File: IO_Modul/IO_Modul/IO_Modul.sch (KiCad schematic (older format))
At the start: 76 parts, among them J101 Conn_02x20_Odd_Even, J102 Screw_Terminal_01x02, J103 Screw_Terminal_01x02, J104 Screw_Terminal_01x02, J105 Screw_Terminal_01x02, J106 Screw_Terminal_01x02, J107 Screw_Terminal_01x02, J108 Screw_Terminal_01x02, J109 Screw_Terminal_01x02, J110 Screw_Terminal_01x02, J111 Screw_Terminal_01x02, J112 Screw_Terminal_01x02, J113 Screw_Terminal_01x02, J114 Screw_Terminal_01x02, J115 Screw_Terminal_01x02, J116 Screw_Terminal_01x02, J117 Screw_Terminal_01x02, J118 Screw_Terminal_01x02, J119 Screw_Terminal_01x02, J120 Screw_Terminal_01x02, J121 Screw_Terminal_01x02, J122 Screw_Terminal_01x02, Q101 Si4431CDY, Q102 Si4431CDY, Q103 Si4431CDY, Q104 Si4431CDY, Q105 Si4431CDY, Q106 2N7002, Q107 2N7002, Q108 2N7002, Q109 2N7002, Q110 2N7002, Q111 Si4431CDY, Q112 Si4431CDY, Q113 Si4431CDY, Q114 Si4431CDY, Q115 Si4431CDY, Q116 2N7002, Q117 2N7002, Q118 2N7002, Q119 2N7002, Q120 2N7002

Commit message: Feeder Microswitch für Tape Motor hinzugefügt. Einige 3D Step Modelle hinzugefügt. Stepper Board die Ecken abgerundet.
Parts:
- J102, J103, J104, J105, J106, J107, J108, J109, J110, J111, J112, J113, J114, J115, J116, J117, J118, J119, J120, J121, J122: footprint TerminalBlock_RND:TerminalBlock_RND_205-00045_1x02_P5.00mm_Horizontal -> ProjectFootprints:TerminalBlock_RND_205-00045_1x02_P5.00mm_Horizontal
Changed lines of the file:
@@
 F 0 "J102" H 1320 785 50  0000 C CNN
 F 1 "Screw_Terminal_01x02" H 1320 876 50  0000 C CNN
-F 2 "TerminalBlock_RND:TerminalBlock_RND_205-00045_1x02_P5.00mm_Horizontal" H 1400 1200 50  0001 C CNN
+F 2 "ProjectFootprints:TerminalBlock_RND_205-00045_1x02_P5.00mm_Horizontal" H 1400 1200 50  0001 C CNN
 F 3 "https://datasheet.lcsc.com/szlcsc/1912251636_Ningbo-Kangnex-Elec-WJ301V-5-0-2P_C8475.pdf" H 1400 1200 50  0001 C CNN
 F 4 "C8475" H 1320 967 50  0000 C CNN "LCSC"
@@
 F 0 "J103" H 1320 1635 50  0000 C CNN
 F 1 "Screw_Terminal_01x02" H 1320 1726 50  0000 C CNN
-F 2 "TerminalBlock_RND:TerminalBlock_RND_205-00045_1x02_P5.00mm_Horizontal" H 1400 2050 50  0001 C CNN
+F 2 "ProjectFootprints:TerminalBlock_RND_205-00045_1x02_P5.00mm_Horizontal" H 1400 2050 50  0001 C CNN
 F 3 "https://datasheet.lcsc.com/szlcsc/1912251636_Ningbo-Kangnex-Elec-WJ301V-5-0-2P_C8475.pdf" H 1400 2050 50  0001 C CNN
 F 4 "C8475" H 1320 1817 50  0000 C CNN "LCSC"
@@
 F 0 "J104" H 1320 2535 50  0000 C CNN
 F 1 "Screw_Terminal_01x02" H 1320 2626 50  0000 C CNN
-F 2 "TerminalBlock_RND:TerminalBlock_RND_205-00045_1x02_P5.00mm_Horizontal" H 1400 2950 50  0001 C CNN
+F 2 "ProjectFootprints:TerminalBlock_RND_205-00045_1x02_P5.00mm_Horizontal" H 1400 2950 50  0001 C CNN
 F 3 "https://datasheet.lcsc.com/szlcsc/1912251636_Ningbo-Kangnex-Elec-WJ301V-5-0-2P_C8475.pdf" H 1400 2950 50  0001 C CNN
 F 4 "C8475" H 1320 2717 50  0000 C CNN "LCSC"
@@
 F 0 "J105" H 1320 3435 50  0000 C CNN
 F 1 "Screw_Terminal_01x02" H 1320 3526 50  0000 C CNN
-F 2 "TerminalBlock_RND:TerminalBlock_RND_205-00045_1x02_P5.00mm_Horizontal" H 1400 3850 50  0001 C CNN
+F 2 "ProjectFootprints:TerminalBlock_RND_205-00045_1x02_P5.00mm_Horizontal" H 1400 3850 50  0001 C CNN
 F 3 "https://datasheet.lcsc.com/szlcsc/1912251636_Ningbo-Kangnex-Elec-WJ301V-5-0-2P_C8475.pdf" H 1400 3850 50  0001 C CNN
 F 4 "C8475" H 1320 3617 50  0000 C CNN "LCSC"
@@
 F 0 "J106" H 1320 4335 50  0000 C CNN
 F 1 "Screw_Terminal_01x02" H 1320 4426 50  0000 C CNN
-F 2 "TerminalBlock_RND:TerminalBlock_RND_205-00045_1x02_P5.00mm_Horizontal" H 1400 4750 50  0001 C CNN
+F 2 "ProjectFootprints:TerminalBlock_RND_205-00045_1x02_P5.00mm_Horizontal" H 1400 4750 50  0001 C CNN
 F 3 "https://datasheet.lcsc.com/szlcsc/1912251636_Ningbo-Kangnex-Elec-WJ301V-5-0-2P_C8475.pdf" H 1400 4750 50  0001 C CNN
 F 4 "C8475" H 1320 4517 50  0000 C CNN "LCSC"
@@
 F 0 "J107" H 2570 785 50  0000 C CNN
 F 1 "Screw_Terminal_01x02" H 2570 876 50  0000 C CNN
-F 2 "TerminalBlock_RND:TerminalBlock_RND_205-00045_1x02_P5.00mm_Horizontal" H 2650 1200 50  0001 C CNN
+F 2 "ProjectFootprints:TerminalBlock_RND_205-00045_1x02_P5.00mm_Horizontal" H 2650 1200 50  0001 C CNN
 F 3 "https://datasheet.lcsc.com/szlcsc/1912251636_Ningbo-Kangnex-Elec-WJ301V-5-0-2P_C8475.pdf" H 2650 1200 50  0001 C CNN
 F 4 "C8475" H 2570 967 50  0000 C CNN "LCSC"
@@
 F 0 "J108" H 2570 1635 50  0000 C CNN
 F 1 "Screw_Terminal_01x02" H 2570 1726 50  0000 C CNN
-F 2 "TerminalBlock_RND:TerminalBlock_RND_205-00045_1x02_P5.00mm_Horizontal" H 2650 2050 50  0001 C CNN
+F 2 "ProjectFootprints:TerminalBlock_RND_205-00045_1x02_P5.00mm_Horizontal" H 2650 2050 50  0001 C CNN
 F 3 "https://datasheet.lcsc.com/szlcsc/1912251636_Ningbo-Kangnex-Elec-WJ301V-5-0-2P_C8475.pdf" H 2650 2050 50  0001 C CNN
 F 4 "C8475" H 2570 1817 50  0000 C CNN "LCSC"
@@
 F 0 "J109" H 2570 2535 50  0000 C CNN
 F 1 "Screw_Terminal_01x02" H 2570 2626 50  0000 C CNN
-F 2 "TerminalBlock_RND:TerminalBlock_RND_205-00045_1x02_P5.00mm_Horizontal" H 2650 2950 50  0001 C CNN
+F 2 "ProjectFootprints:TerminalBlock_RND_205-00045_1x02_P5.00mm_Horizontal" H 2650 2950 50  0001 C CNN
 F 3 "https://datasheet.lcsc.com/szlcsc/1912251636_Ningbo-Kangnex-Elec-WJ301V-5-0-2P_C8475.pdf" H 2650 2950 50  0001 C CNN
 F 4 "C8475" H 2570 2717 50  0000 C CNN "LCSC"
@@
 F 0 "J110" H 2570 3435 50  0000 C CNN
 F 1 "Screw_Terminal_01x02" H 2570 3526 50  0000 C CNN
-F 2 "TerminalBlock_RND:TerminalBlock_RND_205-00045_1x02_P5.00mm_Horizontal" H 2650 3850 50  0001 C CNN
+F 2 "ProjectFootprints:TerminalBlock_RND_205-00045_1x02_P5.00mm_Horizontal" H 2650 3850 50  0001 C CNN
 F 3 "https://datasheet.lcsc.com/szlcsc/1912251636_Ningbo-Kangnex-Elec-WJ301V-5-0-2P_C8475.pdf" H 2650 3850 50  0001 C CNN
 F 4 "C8475" H 2570 3617 50  0000 C CNN "LCSC"
@@
 F 0 "J111" H 2570 4335 50  0000 C CNN
 F 1 "Screw_Terminal_01x02" H 2570 4426 50  0000 C CNN
-F 2 "TerminalBlock_RND:TerminalBlock_RND_205-00045_1x02_P5.00mm_Horizontal" H 2650 4750 50  0001 C CNN
+F 2 "ProjectFootprints:TerminalBlock_RND_205-00045_1x02_P5.00mm_Horizontal" H 2650 4750 50  0001 C CNN
 F 3 "https://datasheet.lcsc.com/szlcsc/1912251636_Ningbo-Kangnex-Elec-WJ301V-5-0-2P_C8475.pdf" H 2650 4750 50  0001 C CNN
 F 4 "C8475" H 2570 4517 50  0000 C CNN "LCSC"
@@
 F 0 "J112" H 4650 1300 50  0000 C CNN
 F 1 "Screw_Terminal_01x02" H 4850 1400 50  0000 C CNN
-F 2 "TerminalBlock_RND:TerminalBlock_RND_205-00045_1x02_P5.00mm_Horizontal" H 4350 1350 50  0001 C CNN
+F 2 "ProjectFootprints:TerminalBlock_RND_205-00045_1x02_P5.00mm_Horizontal" H 4350 1350 50  0001 C CNN
 F 3 "https://datasheet.lcsc.com/szlcsc/1912251636_Ningbo-Kangnex-Elec-WJ301V-5-0-2P_C8475.pdf" H 4350 1350 50  0001 C CNN
 F 4 "C8475" H 4650 1500 50  0000 C CNN "LCSC"
@@
 F 0 "J122" H 9450 450 50  0000 C CNN
 F 1 "Screw_Terminal_01x02" H 9450 550 50  0000 C CNN
-F 2 "TerminalBlock_RND:TerminalBlock_RND_205-00045_1x02_P5.00mm_Horizontal" H 9450 900 50  0001 C CNN
+F 2 "ProjectFootprints:TerminalBlock_RND_205-00045_1x02_P5.00mm_Horizontal" H 9450 900 50  0001 C CNN
 F 3 "https://datasheet.lcsc.com/szlcsc/1912251636_Ningbo-Kangnex-Elec-WJ301V-5-0-2P_C8475.pdf" H 9450 900 50  0001 C CNN
 F 4 "C8475" H 9450 650 50  0000 C CNN "LCSC"
@@
 F 0 "J113" H 4650 2350 50  0000 C CNN
 F 1 "Screw_Terminal_01x02" H 4850 2450 50  0000 C CNN
-F 2 "TerminalBlock_RND:TerminalBlock_RND_205-00045_1x02_P5.00mm_Horizontal" H 4350 2400 50  0001 C CNN
+F 2 "ProjectFootprints:TerminalBlock_RND_205-00045_1x02_P5.00mm_Horizontal" H 4350 2400 50  0001 C CNN
 F 3 "https://datasheet.lcsc.com/szlcsc/1912251636_Ningbo-Kangnex-Elec-WJ301V-5-0-2P_C8475.pdf" H 4350 2400 50  0001 C CNN
 F 4 "C8475" H 4650 2550 50  0000 C CNN "LCSC"
@@
 F 0 "J114" H 4650 3400 50  0000 C CNN
 F 1 "Screw_Terminal_01x02" H 4850 3500 50  0000 C CNN
-F 2 "TerminalBlock_RND:TerminalBlock_RND_205-00045_1x02_P5.00mm_Horizontal" H 4350 3450 50  0001 C CNN
+F 2 "ProjectFootprints:TerminalBlock_RND_205-00045_1x02_P5.00mm_Horizontal" H 4350 3450 50  0001 C CNN
 F 3 "https://datasheet.lcsc.com/szlcsc/1912251636_Ningbo-Kangnex-Elec-WJ301V-5-0-2P_C8475.pdf" H 4350 3450 50  0001 C CNN
 F 4 "C8475" H 4650 3600 50  0000 C CNN "LCSC"
@@
 F 0 "J115" H 4650 4400 50  0000 C CNN
 F 1 "Screw_Terminal_01x02" H 4850 4500 50  0000 C CNN
-F 2 "TerminalBlock_RND:TerminalBlock_RND_205-00045_1x02_P5.00mm_Horizontal" H 4350 4450 50  0001 C CNN
+F 2 "ProjectFootprints:TerminalBlock_RND_205-00045_1x02_P5.00mm_Horizontal" H 4350 4450 50  0001 C CNN
 F 3 "https://datasheet.lcsc.com/szlcsc/1912251636_Ningbo-Kangnex-Elec-WJ301V-5-0-2P_C8475.pdf" H 4350 4450 50  0001 C CNN
 F 4 "C8475" H 4650 4600 50  0000 C CNN "LCSC"
@@
 F 0 "J116" H 4650 5450 50  0000 C CNN
 F 1 "Screw_Terminal_01x02" H 4850 5550 50  0000 C CNN
-F 2 "TerminalBlock_RND:TerminalBlock_RND_205-00045_1x02_P5.00mm_Horizontal" H 4350 5500 50  0001 C CNN
+F 2 "ProjectFootprints:TerminalBlock_RND_205-00045_1x02_P5.00mm_Horizontal" H 4350 5500 50  0001 C CNN
 F 3 "https://datasheet.lcsc.com/szlcsc/1912251636_Ningbo-Kangnex-Elec-WJ301V-5-0-2P_C8475.pdf" H 4350 5500 50  0001 C CNN
 F 4 "C8475" H 4650 5650 50  0000 C CNN "LCSC"
@@
 F 0 "J117" H 6950 1300 50  0000 C CNN
 F 1 "Screw_Terminal_01x02" H 7150 1400 50  0000 C CNN
-F 2 "TerminalBlock_RND:TerminalBlock_RND_205-00045_1x02_P5.00mm_Horizontal" H 6650 1350 50  0001 C CNN
+F 2 "ProjectFootprints:TerminalBlock_RND_205-00045_1x02_P5.00mm_Horizontal" H 6650 1350 50  0001 C CNN
 F 3 "https://datasheet.lcsc.com/szlcsc/1912251636_Ningbo-Kangnex-Elec-WJ301V-5-0-2P_C8475.pdf" H 6650 1350 50  0001 C CNN
 F 4 "C8475" H 6950 1500 50  0000 C CNN "LCSC"
@@
 F 0 "J118" H 6950 2350 50  0000 C CNN
 F 1 "Screw_Terminal_01x02" H 7150 2450 50  0000 C CNN
-F 2 "TerminalBlock_RND:TerminalBlock_RND_205-00045_1x02_P5.00mm_Horizontal" H 6650 2400 50  0001 C CNN
+F 2 "ProjectFootprints:TerminalBlock_RND_205-00045_1x02_P5.00mm_Horizontal" H 6650 2400 50  0001 C CNN
 F 3 "https://datasheet.lcsc.com/szlcsc/1912251636_Ningbo-Kangnex-Elec-WJ301V-5-0-2P_C8475.pdf" H 6650 2400 50  0001 C CNN
 F 4 "C8475" H 6950 2550 50  0000 C CNN "LCSC"
@@
 F 0 "J119" H 6950 3400 50  0000 C CNN
 F 1 "Screw_Terminal_01x02" H 7150 3500 50  0000 C CNN
-F 2 "TerminalBlock_RND:TerminalBlock_RND_205-00045_1x02_P5.00mm_Horizontal" H 6650 3450 50  0001 C CNN
+F 2 "ProjectFootprints:TerminalBlock_RND_205-00045_1x02_P5.00mm_Horizontal" H 6650 3450 50  0001 C CNN
 F 3 "https://datasheet.lcsc.com/szlcsc/1912251636_Ningbo-Kangnex-Elec-WJ301V-5-0-2P_C8475.pdf" H 6650 3450 50  0001 C CNN
 F 4 "C8475" H 6950 3600 50  0000 C CNN "LCSC"
@@
 F 0 "J120" H 6950 4400 50  0000 C CNN
 F 1 "Screw_Terminal_01x02" H 7150 4500 50  0000 C CNN
-F 2 "TerminalBlock_RND:TerminalBlock_RND_205-00045_1x02_P5.00mm_Horizontal" H 6650 4450 50  0001 C CNN
+F 2 "ProjectFootprints:TerminalBlock_RND_205-00045_1x02_P5.00mm_Horizontal" H 6650 4450 50  0001 C CNN
 F 3 "https://datasheet.lcsc.com/szlcsc/1912251636_Ningbo-Kangnex-Elec-WJ301V-5-0-2P_C8475.pdf" H 6650 4450 50  0001 C CNN
 F 4 "C8475" H 6950 4600 50  0000 C CNN "LCSC"
@@
 F 0 "J121" H 6950 5450 50  0000 C CNN
 F 1 "Screw_Terminal_01x02" H 7150 5550 50  0000 C CNN
-F 2 "TerminalBlock_RND:TerminalBlock_RND_205-00045_1x02_P5.00mm_Horizontal" H 6650 5500 50  0001 C CNN
+F 2 "ProjectFootprints:TerminalBlock_RND_205-00045_1x02_P5.00mm_Horizontal" H 6650 5500 50  0001 C CNN
 F 3 "https://datasheet.lcsc.com/szlcsc/1912251636_Ningbo-Kangnex-Elec-WJ301V-5-0-2P_C8475.pdf" H 6650 5500 50  0001 C CNN
 F 4 "C8475" H 6950 5650 50  0000 C CNN "LCSC"

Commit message: BOM für LCSC überarbeitet. Tool für BOM export modifiziert
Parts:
- H101, H102, H103, H104: LCSC (none) -> 0
- J101: LCSC (none) -> C601944
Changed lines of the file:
@@
 F 2 "MountingHole:MountingHole_3.2mm_M3_Pad_Via" H 1150 7050 50  0001 C CNN
 F 3 "~" H 1150 7050 50  0001 C CNN
+F 4 "0" H 1150 7050 50  0001 C CNN "LCSC"
 	1    1150 7050
 	0    1    1    0
@@
 F 2 "MountingHole:MountingHole_3.2mm_M3_Pad_Via" H 1150 6650 50  0001 C CNN
 F 3 "~" H 1150 6650 50  0001 C CNN
+F 4 "0" H 1150 6650 50  0001 C CNN "LCSC"
 	1    1150 6650
 	0    1    1    0
@@
 F 2 "MountingHole:MountingHole_3.2mm_M3_Pad_Via" H 1150 6850 50  0001 C CNN
 F 3 "~" H 1150 6850 50  0001 C CNN
+F 4 "0" H 1150 6850 50  0001 C CNN "LCSC"
 	1    1150 6850
 	0    1    1    0
@@
 F 2 "MountingHole:MountingHole_3.2mm_M3_Pad_Via" H 1150 7250 50  0001 C CNN
 F 3 "~" H 1150 7250 50  0001 C CNN
+F 4 "0" H 1150 7250 50  0001 C CNN "LCSC"
 	1    1150 7250
 	0    1    1    0
@@
 F 2 "Connector_PinHeader_2.54mm:PinHeader_2x20_P2.54mm_Vertical" H 9650 4350 50  0001 C CNN
 F 3 "~" H 9650 4350 50  0001 C CNN
+F 4 "C601944" H 9650 4350 50  0001 C CNN "LCSC"
 	1    9650 4350
 	1    0    0    -1

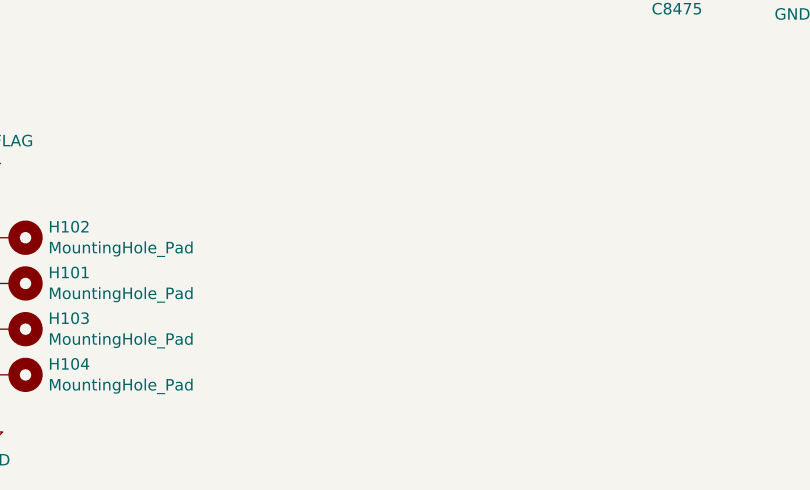
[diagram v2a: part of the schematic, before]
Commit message: Fiducials auf allen Boards hinzugefügt
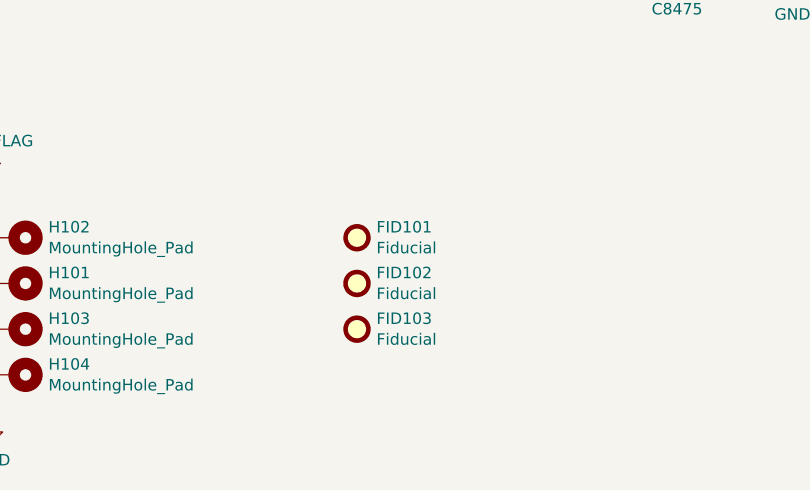
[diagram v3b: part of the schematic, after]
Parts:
- added FID101, FID102, FID103: Fiducial, Fiducial:Fiducial_1mm_Mask2mm, symbol Mechanical:Fiducial
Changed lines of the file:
@@
 	-1   0    0    1
 $EndComp
+$Comp
+L Mechanical:Fiducial FID101
+U 1 1 602B2FA0
+P 2650 6650
+F 0 "FID101" H 2735 6696 50  0000 L CNN
+F 1 "Fiducial" H 2735 6605 50  0000 L CNN
+F 2 "Fiducial:Fiducial_1mm_Mask2mm" H 2650 6650 50  0001 C CNN
+F 3 "~" H 2650 6650 50  0001 C CNN
+	1    2650 6650
+	1    0    0    -1
+$EndComp
+$Comp
+L Mechanical:Fiducial FID102
+U 1 1 602B428B
+P 2650 6850
+F 0 "FID102" H 2735 6896 50  0000 L CNN
+F 1 "Fiducial" H 2735 6805 50  0000 L CNN
+F 2 "Fiducial:Fiducial_1mm_Mask2mm" H 2650 6850 50  0001 C CNN
+F 3 "~" H 2650 6850 50  0001 C CNN
+	1    2650 6850
+	1    0    0    -1
+$EndComp
+$Comp
+L Mechanical:Fiducial FID103
+U 1 1 602B49FA
+P 2650 7050
+F 0 "FID103" H 2735 7096 50  0000 L CNN
+F 1 "Fiducial" H 2735 7005 50  0000 L CNN
+F 2 "Fiducial:Fiducial_1mm_Mask2mm" H 2650 7050 50  0001 C CNN
+F 3 "~" H 2650 7050 50  0001 C CNN
+	1    2650 7050
+	1    0    0    -1
+$EndComp
 $EndSCHEMATC

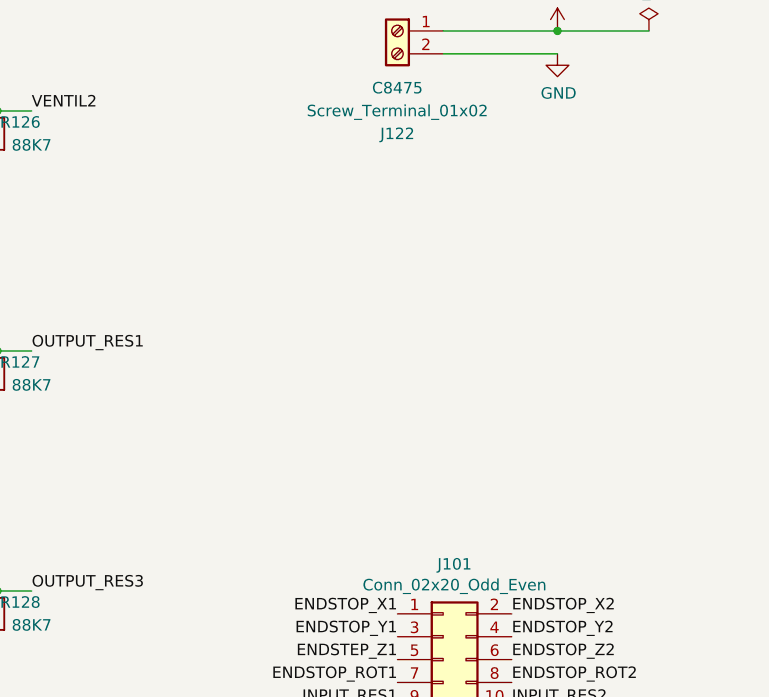
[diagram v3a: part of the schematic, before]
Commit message: ESD Protection überarbeitet, aber noch nicht fertig
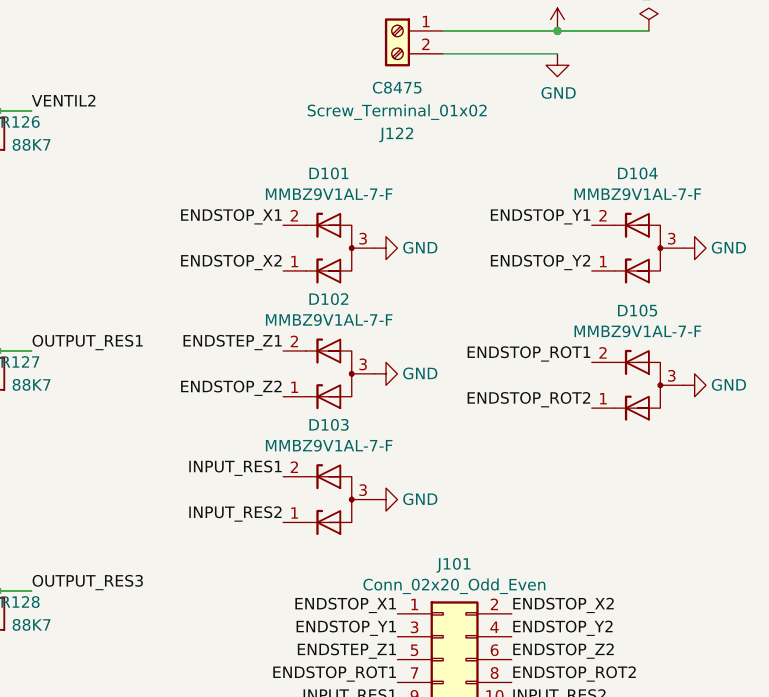
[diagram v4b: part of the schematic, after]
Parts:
- added D101, D102, D103, D104, D105: MMBZ9V1AL-7-F, Package_TO_SOT_SMD:SOT-23, symbol Diode:MMBZxx
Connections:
- net ENDSTEP_Z1: now also D102.2 (K)
- net ENDSTOP_ROT1: now also D105.2 (K)
- net ENDSTOP_ROT2: now also D105.1 (K)
- net ENDSTOP_X1: now also D101.2 (K)
- net ENDSTOP_X2: now also D101.1 (K)
- net ENDSTOP_Y1: now also D104.2 (K)
- net ENDSTOP_Y2: now also D104.1 (K)
- net ENDSTOP_Z2: now also D102.1 (K)
- net GND: now also D101.3 (A), D102.3 (A), D103.3 (A), D104.3 (A), D105.3 (A)
- net INPUT_RES1: now also D103.2 (K)
- net INPUT_RES2: now also D103.1 (K)
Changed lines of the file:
@@
 	1    0    0    -1
 $EndComp
+$Comp
+L Diode:MMBZxx D101
+U 1 1 604C99B2
+P 9150 1850
+F 0 "D101" V 9475 1850 50  0000 C CNN
+F 1 "MMBZ9V1AL-7-F" V 9384 1850 50  0000 C CNN
+F 2 "Package_TO_SOT_SMD:SOT-23" H 9300 1750 50  0001 L CNN
+F 3 "http://www.onsemi.com/pub/Collateral/MMBZ5V6ALT1-D.PDF" V 9050 1850 50  0001 C CNN
+F 4 "C460913" V 9150 1850 50  0001 C CNN "LCSC"
+	1    9150 1850
+	0    -1   -1   0
+$EndComp
+$Comp
+L Diode:MMBZxx D104
+U 1 1 604F9147
+P 10500 1850
+F 0 "D104" V 10825 1850 50  0000 C CNN
+F 1 "MMBZ9V1AL-7-F" V 10734 1850 50  0000 C CNN
+F 2 "Package_TO_SOT_SMD:SOT-23" H 10650 1750 50  0001 L CNN
+F 3 "http://www.onsemi.com/pub/Collateral/MMBZ5V6ALT1-D.PDF" V 10400 1850 50  0001 C CNN
+F 4 "C460913" V 10500 1850 50  0001 C CNN "LCSC"
+	1    10500 1850
+	0    -1   -1   0
+$EndComp
+$Comp
+L Diode:MMBZxx D102
+U 1 1 604FA938
+P 9150 2400
+F 0 "D102" V 9475 2400 50  0000 C CNN
+F 1 "MMBZ9V1AL-7-F" V 9384 2400 50  0000 C CNN
+F 2 "Package_TO_SOT_SMD:SOT-23" H 9300 2300 50  0001 L CNN
+F 3 "http://www.onsemi.com/pub/Collateral/MMBZ5V6ALT1-D.PDF" V 9050 2400 50  0001 C CNN
+F 4 "C460913" V 9150 2400 50  0001 C CNN "LCSC"
+	1    9150 2400
+	0    -1   -1   0
+$EndComp
+$Comp
+L Diode:MMBZxx D105
+U 1 1 604FC64F
+P 10500 2450
+F 0 "D105" V 10825 2450 50  0000 C CNN
+F 1 "MMBZ9V1AL-7-F" V 10734 2450 50  0000 C CNN
+F 2 "Package_TO_SOT_SMD:SOT-23" H 10650 2350 50  0001 L CNN
+F 3 "http://www.onsemi.com/pub/Collateral/MMBZ5V6ALT1-D.PDF" V 10400 2450 50  0001 C CNN
+F 4 "C460913" V 10500 2450 50  0001 C CNN "LCSC"
+	1    10500 2450
+	0    -1   -1   0
+$EndComp
+$Comp
+L Diode:MMBZxx D103
+U 1 1 604FDFEA
+P 9150 2950
+F 0 "D103" V 9475 2950 50  0000 C CNN
+F 1 "MMBZ9V1AL-7-F" V 9384 2950 50  0000 C CNN
+F 2 "Package_TO_SOT_SMD:SOT-23" H 9300 2850 50  0001 L CNN
+F 3 "http://www.onsemi.com/pub/Collateral/MMBZ5V6ALT1-D.PDF" V 9050 2950 50  0001 C CNN
+F 4 "C460913" V 9150 2950 50  0001 C CNN "LCSC"
+	1    9150 2950
+	0    -1   -1   0
+$EndComp
+Text Label 8950 1750 2    50   ~ 0
+ENDSTOP_X1
+Text Label 8950 1950 2    50   ~ 0
+ENDSTOP_X2
+Text Label 10300 1750 2    50   ~ 0
+ENDSTOP_Y1
+Text Label 10300 1950 2    50   ~ 0
+ENDSTOP_Y2
+Text Label 8950 2300 2    50   ~ 0
+ENDSTEP_Z1
+Text Label 8950 2500 2    50   ~ 0
+ENDSTOP_Z2
+Text Label 10300 2350 2    50   ~ 0
+ENDSTOP_ROT1
+Text Label 10300 2550 2    50   ~ 0
+ENDSTOP_ROT2
+Text Label 8950 2850 2    50   ~ 0
+INPUT_RES1
+Text Label 8950 3050 2    50   ~ 0
+INPUT_RES2
+$Comp
+L power:GND #PWR0164
+U 1 1 605B04A9
+P 9350 2950
+F 0 "#PWR0164" H 9350 2700 50  0001 C CNN
+F 1 "GND" V 9350 2750 50  0000 C CNN
+F 2 "" H 9350 2950 50  0001 C CNN
+F 3 "" H 9350 2950 50  0001 C CNN
+	1    9350 2950
+	0    -1   -1   0
+$EndComp
+$Comp
+L power:GND #PWR0165
+U 1 1 605B1C11
+P 9350 2400
+F 0 "#PWR0165" H 9350 2150 50  0001 C CNN
+F 1 "GND" V 9350 2200 50  0000 C CNN
+F 2 "" H 9350 2400 50  0001 C CNN
+F 3 "" H 9350 2400 50  0001 C CNN
+	1    9350 2400
+	0    -1   -1   0
+$EndComp
+$Comp
+L power:GND #PWR0166
+U 1 1 605B32CE
+P 9350 1850
+F 0 "#PWR0166" H 9350 1600 50  0001 C CNN
+F 1 "GND" V 9350 1650 50  0000 C CNN
+F 2 "" H 9350 1850 50  0001 C CNN
+F 3 "" H 9350 1850 50  0001 C CNN
+	1    9350 1850
+	0    -1   -1   0
+$EndComp
+$Comp
+L power:GND #PWR0167
+U 1 1 605B49DF
+P 10700 1850
+F 0 "#PWR0167" H 10700 1600 50  0001 C CNN
+F 1 "GND" V 10700 1650 50  0000 C CNN
+F 2 "" H 10700 1850 50  0001 C CNN
+F 3 "" H 10700 1850 50  0001 C CNN
+	1    10700 1850
+	0    -1   -1   0
+$EndComp
+$Comp
+L power:GND #PWR0168
+U 1 1 605B6172
+P 10700 2450
+F 0 "#PWR0168" H 10700 2200 50  0001 C CNN
+F 1 "GND" V 10700 2250 50  0000 C CNN
+F 2 "" H 10700 2450 50  0001 C CNN
+F 3 "" H 10700 2450 50  0001 C CNN
+	1    10700 2450
+	0    -1   -1   0
+$EndComp
 $EndSCHEMATC

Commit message: Änderungen für bestellung V01 -  Bestellung abgeschickt
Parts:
- added D106, D107: MMBZ9V1AL-7-F, Package_TO_SOT_SMD:SOT-23, symbol Diode:MMBZxx
- added J123, J124, J125, J126: Screw_Terminal_01x03, TerminalBlock_RND:TerminalBlock_RND_205-00046_1x03_P5.00mm_Horizontal, symbol Connector:Screw_Terminal_01x03
- FID101, FID102, FID103: LCSC (none) -> 0
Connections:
- net +3V3: now also J123.1 (Pin_1), J124.1 (Pin_1), J125.1 (Pin_1), J126.1 (Pin_1)
- net ADC_RES1: now also D107.2 (K), J123.2 (Pin_2)
- net ADC_RES2: now also D107.1 (K), J124.2 (Pin_2)
- net ADC_RES3: now also D106.2 (K), J125.2 (Pin_2)
- net ADC_RES4: now also D106.1 (K), J126.2 (Pin_2)
- net GND: now also D106.3 (A), D107.3 (A), J123.3 (Pin_3), J124.3 (Pin_3), J125.3 (Pin_3), J126.3 (Pin_3)
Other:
- moved on the sheet: J101
